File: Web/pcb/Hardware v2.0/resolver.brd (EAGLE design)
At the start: 39 x 31.7 mm, 17 parts, among them IC1 LM386N-1

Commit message: software updates
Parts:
- added C10: 22n, rcl:C050-024X044
- C9: value 47n -> 22n; device rcl:C025-024X044 -> rcl:C050-024X044
- moved C9 1.52 mm to (50.5, 41.9), turned to 270 degrees
- moved R5 1.05 mm to (63.2, 54.9)
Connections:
- new net N$6: C10.1, C9.1, R6.2
- net N$1: now also C10.2; no longer C9.1, R6.2
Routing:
- net N$6: track 0.00 -> 15.6 mm
- net N$1: track 38.7 -> 24.0 mm
- net +12V: track 53.8 -> 51.6 mm
- net R1: track 12.8 -> 14.5 mm

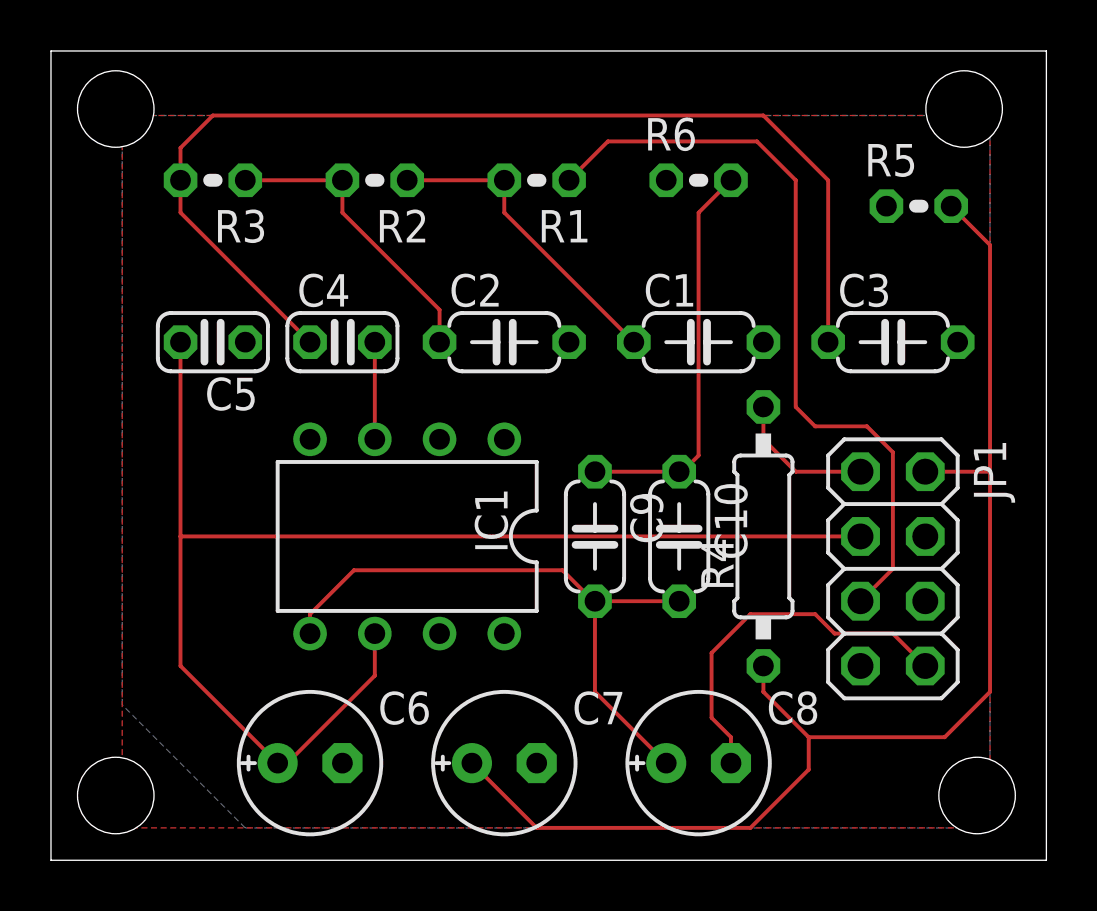
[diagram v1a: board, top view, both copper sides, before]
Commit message: optimized icons
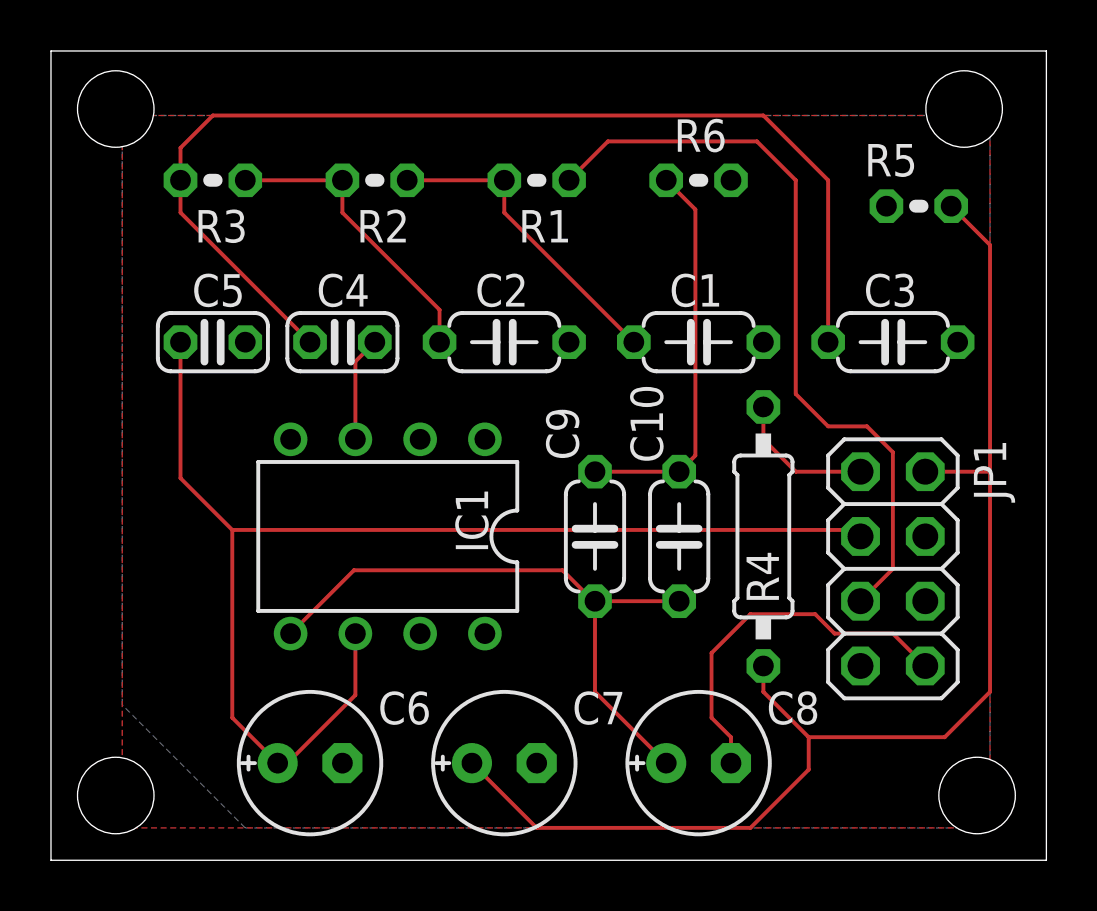
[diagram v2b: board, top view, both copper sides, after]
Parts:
- moved IC1 0.76 mm to (42.4, 41.9)
- turned R6 to 180 degrees
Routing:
- net +12V: track 51.6 -> 49.4 mm
